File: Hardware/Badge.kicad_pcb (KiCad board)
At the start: 2 copper layers, 100 x 100 mm, 116 parts, among them J1 Battery_Conn, J2 Conn_01x02, J3 DEBUG, J4 Conn_02x15_Counter_Clockwise, J5 Conn_01x12, P1 USB_C_Plug_USB2.0, Q1 SI1967DH-T1-GE3, Q2 2SC4213, SW1 BOOT_MODE, SW2 RESET, SW3 PWR_BATT, SW4 SEL_BATT, SW5 Button B, SW6 Button A, U1 W25Q128JVS, U2 MCP73832-2-OT, U3 LD1117S33TR_SOT223, U4 RP2040, U5 BHI160B, U6 BMM150, U7 ESP32-S3-WROOM-1, Y1 12MHz_GND24

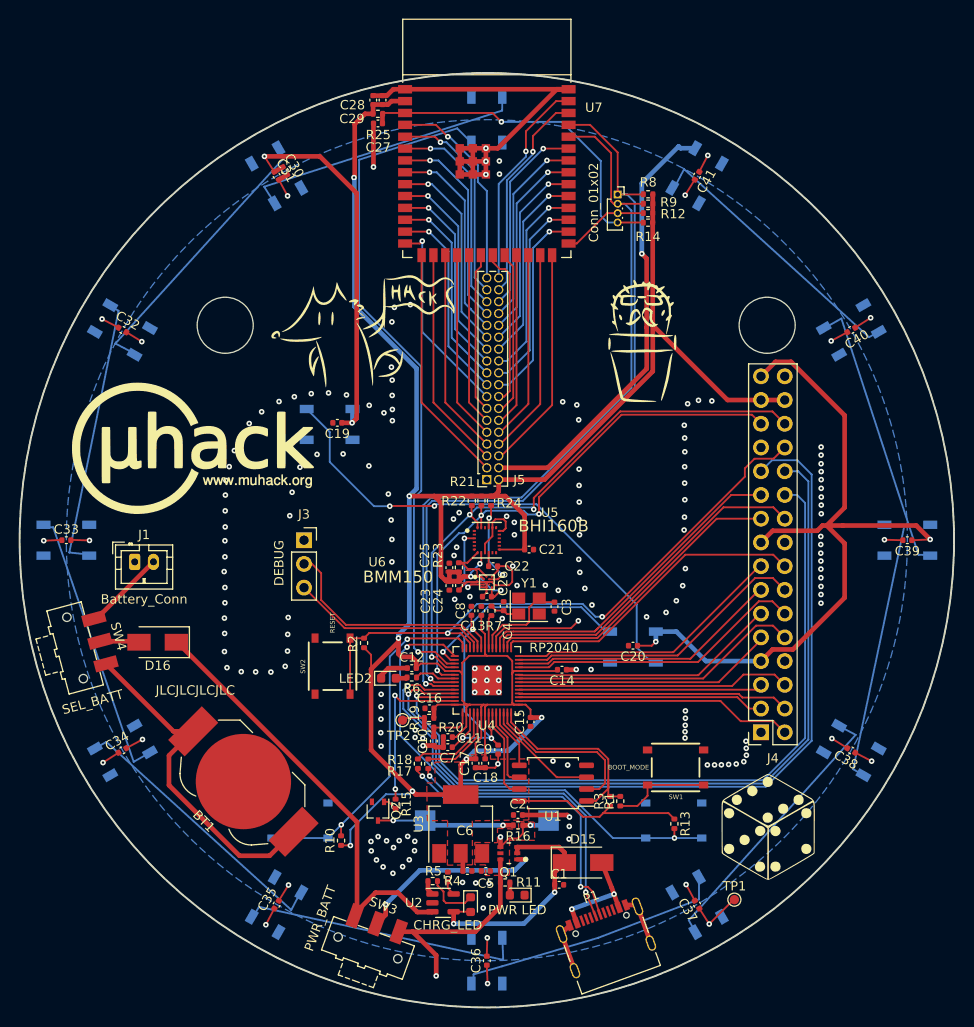
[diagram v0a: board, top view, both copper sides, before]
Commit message: Added SAOv2 Connector - re-arranged some RP pins connection
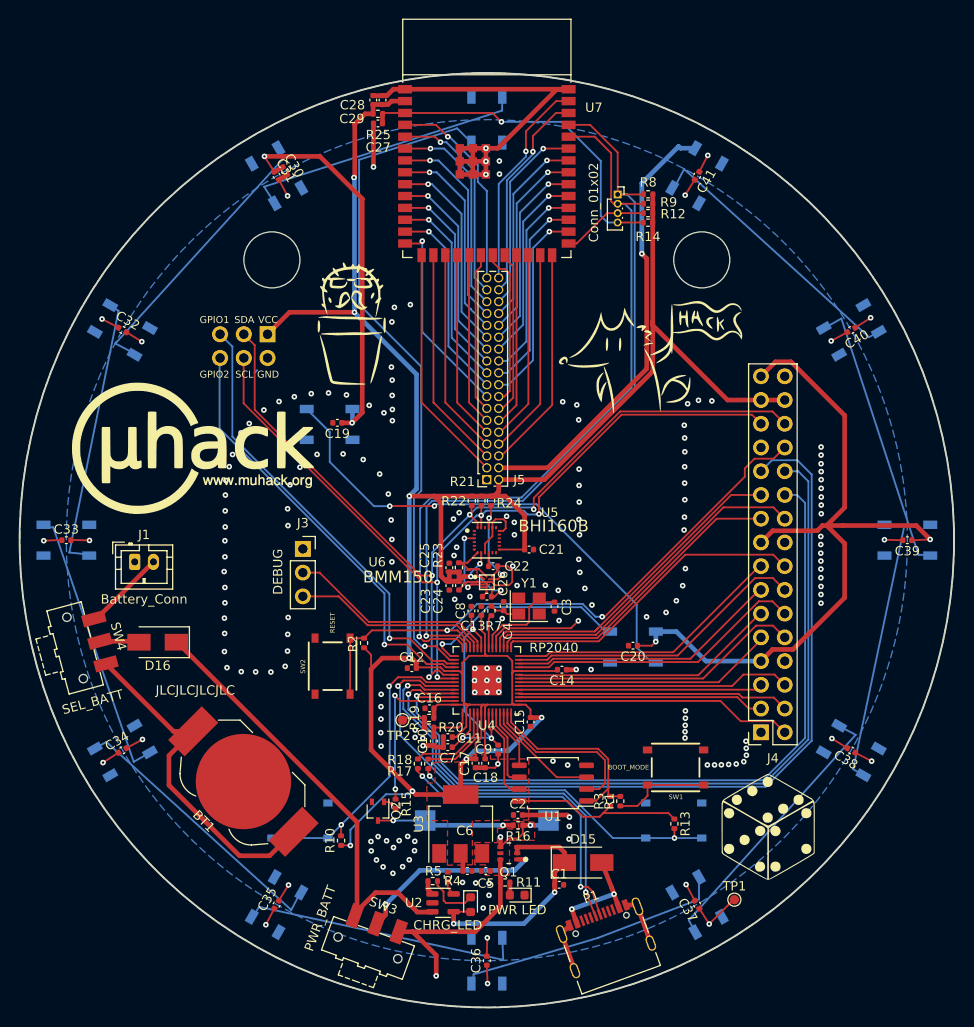
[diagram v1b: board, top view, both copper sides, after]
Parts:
- removed LED2: USR LED, LED_SMD:LED_0603_1608Metric
- removed R6: 470, Resistor_SMD:R_0402_1005Metric
- added X1: SAOv2, SAOv2:Simple_Addon_v2-BADGE-2x3, B.Cu at (74.0, 79.2)
- moved G*** 31.2 mm to (84.9, 76.8)
- moved G*** 30.9 mm to (117.5, 80.4)
- moved J3 0.94 mm to (80.3, 100.9)
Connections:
- J2 pad 1: /GPIO24 -> /ESP_TX
- J2 pad 2: /GPIO25 -> /ESP_RX
- R8 pad 1: /GPIO24 -> /ESP_TX
- R9 pad 1: /GPIO25 -> /ESP_RX
- U4 pad 27: /GPIO_16 -> /ESP_TX
- U4 pad 28: /SW_1 -> /ESP_RX
- U4 pad 29: /SW_2 -> /LED_POST
- U4 pad 30: /LED_POST -> /LED_STRIPE
- U4 pad 31: /LED_STRIPE -> /SAO_1
- U4 pad 32: /I2C_SDA -> /SAO_2
- U4 pad 34: /I2C_SCL -> /I2C_SDA
- U4 pad 35: /GPIO23 -> /I2C_SCL
- U4 pad 36: /GPIO24 -> /SW_1
- U4 pad 37: /GPIO25 -> /SW_2
- U7 pad 36: /GPIO25 -> /ESP_RX
- U7 pad 37: /GPIO24 -> /ESP_TX
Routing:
- net /GPIO24: track 84.7 -> 0.00 mm, vias 1 -> 0
- net /GPIO25: track 84.6 -> 0.00 mm, vias 1 -> 0
- net /ESP_TX: track 0.00 -> 82.4 mm, vias 0 -> 1
- net /ESP_RX: track 0.00 -> 82.0 mm, vias 0 -> 1
- net /SAO_1: track 0.00 -> 48.2 mm, vias 0 -> 1
- net /SAO_2: track 0.00 -> 46.5 mm, vias 0 -> 1
- net /I2C_SDA: track 62.4 -> 99.8 mm, vias 3 -> 4
- net /I2C_SCL: track 59.5 -> 93.5 mm, vias 3 -> 4
- net +3V3: track 311.9 -> 320.4 mm, vias 10 -> 11
- net /SW_1: track 38.7 -> 33.8 mm
- net /GPIO23: track 4.48 -> 0.00 mm
- net /SW_2: track 53.3 -> 49.8 mm
- net GND: track 135.2 -> 132.2 mm, vias 188 -> 190
- net /SWCLK: track 24.4 -> 22.5 mm
- net Net-(LED2-Pad2): track 1.23 -> 0.00 mm
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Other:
- outline, holes or cut-outs redrawn

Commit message: Connected both USB-C data signal, moved the crystal - revisisted ready for production
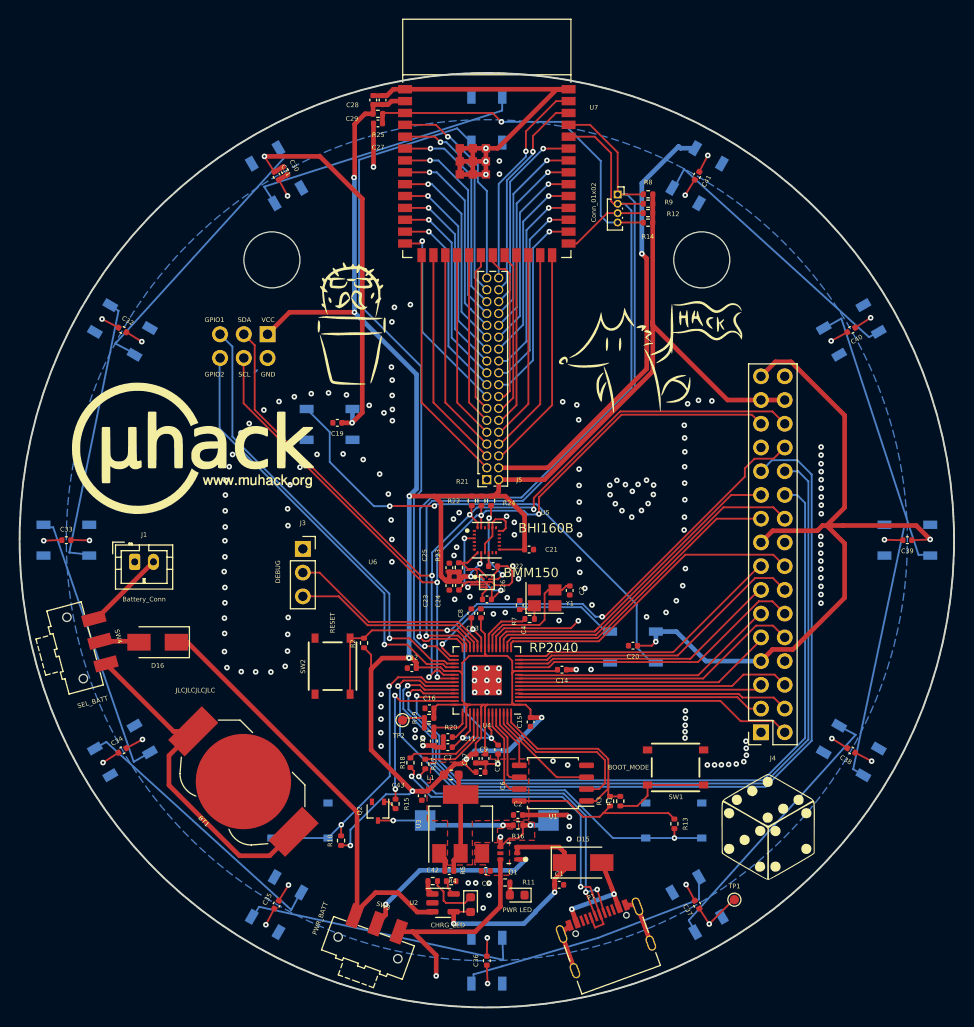
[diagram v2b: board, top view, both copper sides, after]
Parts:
- added C42: 100n, Capacitor_SMD:C_0402_1005Metric, F.Cu at (96.0, 135.4)
- added C43: 10n, Capacitor_SMD:C_0402_1005Metric, F.Cu at (93.0, 127.3)
- added L1: 330H-1.7A, Inductor_SMD:L_0603_1608Metric, F.Cu at (96.2, 125.1)
- C6: value 10u -> 100n
- X1: value SAOv2 -> Simple_Addon_v2
- moved C6 10.7 mm to (99.3, 124.8)
- moved R7 4.18 mm to (104.6, 108.4), turned to 180 degrees
- moved C3 2.38 mm to (108.9, 105.4)
- moved Y1 1.90 mm to (106.2, 106.2)
- moved C4 1.72 mm to (103.5, 106.9)
- moved R18 0.81 mm to (91.8, 123.8)
- moved R5 0.58 mm to (96.2, 136.5), turned to 180 degrees
- moved C18 0.52 mm to (99.9, 123.3)
- moved C17 0.51 mm to (98.8, 123.4)
- moved R17 0.32 mm to (93.4, 124.0)
- moved C26 0.30 mm to (100.0, 106.3)
- moved C13 0.27 mm to (99.4, 107.8)
- moved C8 0.27 mm to (98.3, 107.8)
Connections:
- P1 pad A8: (no net) -> unconnected-(P1-PadA8)
- P1 pad B6: (no net) -> /USB_D+
- P1 pad B7: (no net) -> /USB_D-
- P1 pad B8: (no net) -> unconnected-(P1-PadB8)
- U3 pad 2: +3V3 -> Net-(C42-Pad2)
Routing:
- net Net-(C42-Pad2): track 0.00 -> 11.0 mm
- net /USB_D+: track 30.2 -> 35.5 mm, vias 2 -> 3
- net /USB_D-: track 31.5 -> 36.1 mm
- net GND: track 132.2 -> 135.4 mm
- net +3V3: track 320.4 -> 317.6 mm
- net /XIN: track 10.8 -> 13.5 mm
- net /XOUT: track 3.61 -> 6.06 mm
- net Net-(R18-Pad1): track 9.51 -> 10.3 mm
- net Net-(D16-Pad1): track 47.8 -> 48.4 mm
